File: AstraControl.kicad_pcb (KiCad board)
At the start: 4 copper layers, 110 x 96 mm, 149 parts, among them CN1 4P JST VH, CN10 JST_ZH_6PIN_1A_250V, CN2 4P JST VH, CN3 4P JST VH, CN4 4P JST ZH, CN5 4P JST ZH, CN6 4P JST ZH, CN7 JST_VH_8PIN_10A_250V, CN8 4P JST ZH, CN9 4P JST ZH, SW1 TS_Basic_Small, SW2 TS_Basic_Small, U1 ESP32-S3-WROOM-1U-N8, U2 NCP361SNT1G, U3 ST1S12GR, U4 USBLC6, U5 SN65HVD1782DR, U6 TXB0104PWR

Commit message: commit before updating to LiveAstra lib
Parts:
- removed H1, H2, H3, H4: MountingHole_Pad, MountingHole:MountingHole_5.3mm_M5_DIN965_Pad
- removed TP16, TP17: TestPoint_Thimble, TestPoint:TestPoint_Loop_D3.50mm_Drill0.9mm_Beaded
- added G1: ~, EASYEDA2KICAD:AstraControl_Ground_Band, F.Cu at (158.0, 108.0)
- added R9: 10k, Resistor_SMD:R_0402_1005Metric, F.Cu at (170.5, 143.0)
- moved R34 143.0 mm to (109.0, 80.0), turned to 180 degrees
- moved C23 137.9 mm to (109.0, 82.0), turned to 180 degrees
- moved R36 132.4 mm to (107.5, 138.0)
- moved R33 127.5 mm to (162.5, 142.5), turned to 90 degrees
- moved C25 127.5 mm to (107.5, 141.0)
- moved TP64 125.3 mm to (149.5, 142.5)
- moved C22 124.3 mm to (167.5, 143.5), turned to 90 degrees
- moved R32 123.6 mm to (165.5, 143.5), turned to 90 degrees
- moved TP18 118.7 mm to (116.5, 76.0)
- moved TP55 114.0 mm to (191.0, 78.5)
- moved TP59 110.2 mm to (178.0, 81.0)
- moved TP60 109.6 mm to (148.0, 135.0)
- moved TP56 107.7 mm to (183.0, 81.5)
- moved TP57 107.3 mm to (188.5, 82.0)
- moved TP1 106.9 mm to (130.0, 112.0)
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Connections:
- net Net-(CN9-Pad4) renamed /Block Diagram/Button, Status LED, UART and I2S/STATUS_LED_CONN
- net Net-(U1-IO3) renamed /Block Diagram/MCU/IO_3_IC
- CN9 pad 2: /Block Diagram/Button, Status LED, UART and I2S/GPIO_12_BUTTON -> Net-(CN9-Pad2)
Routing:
- net CHASSIS: track 0.00 -> 6.80 mm
- net GND: track 0.00 -> 0.58 mm
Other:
- outline, holes or cut-outs redrawn

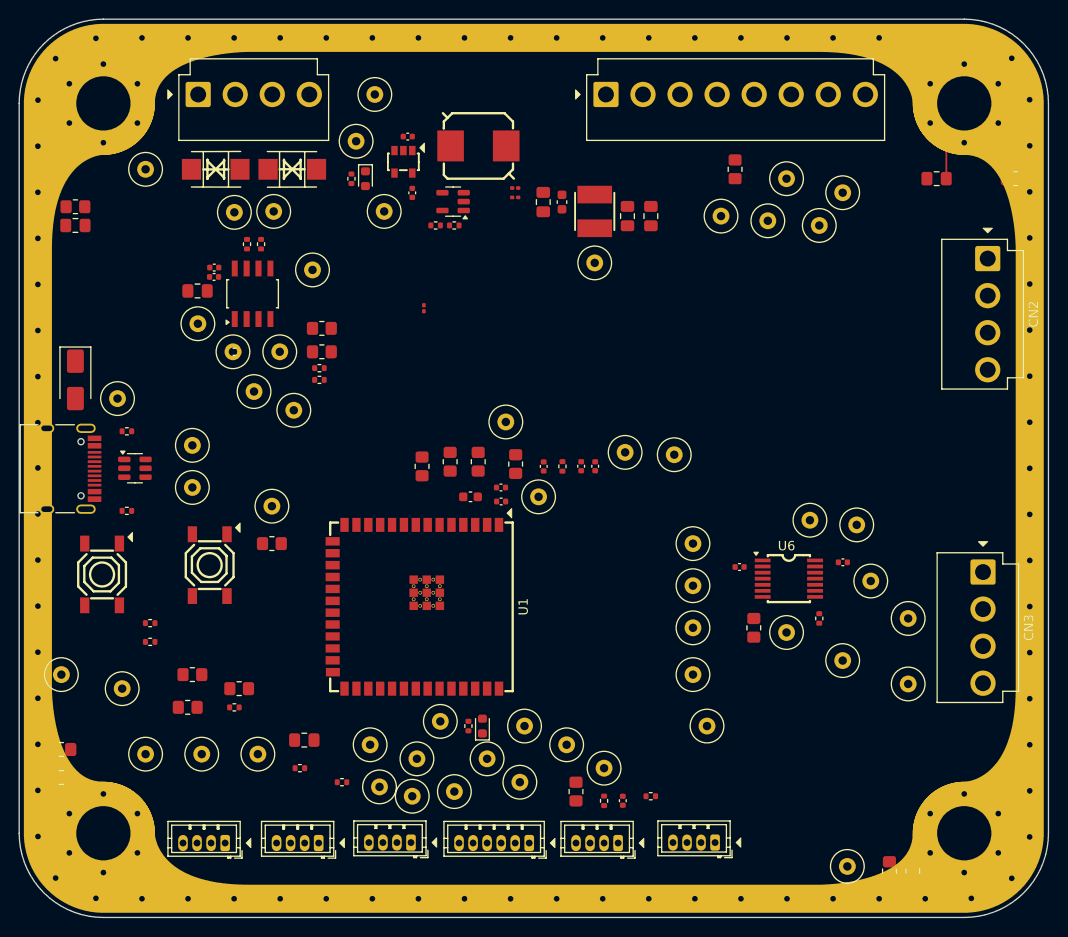
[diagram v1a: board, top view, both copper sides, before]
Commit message: Updated library name, updated and verified all footprints
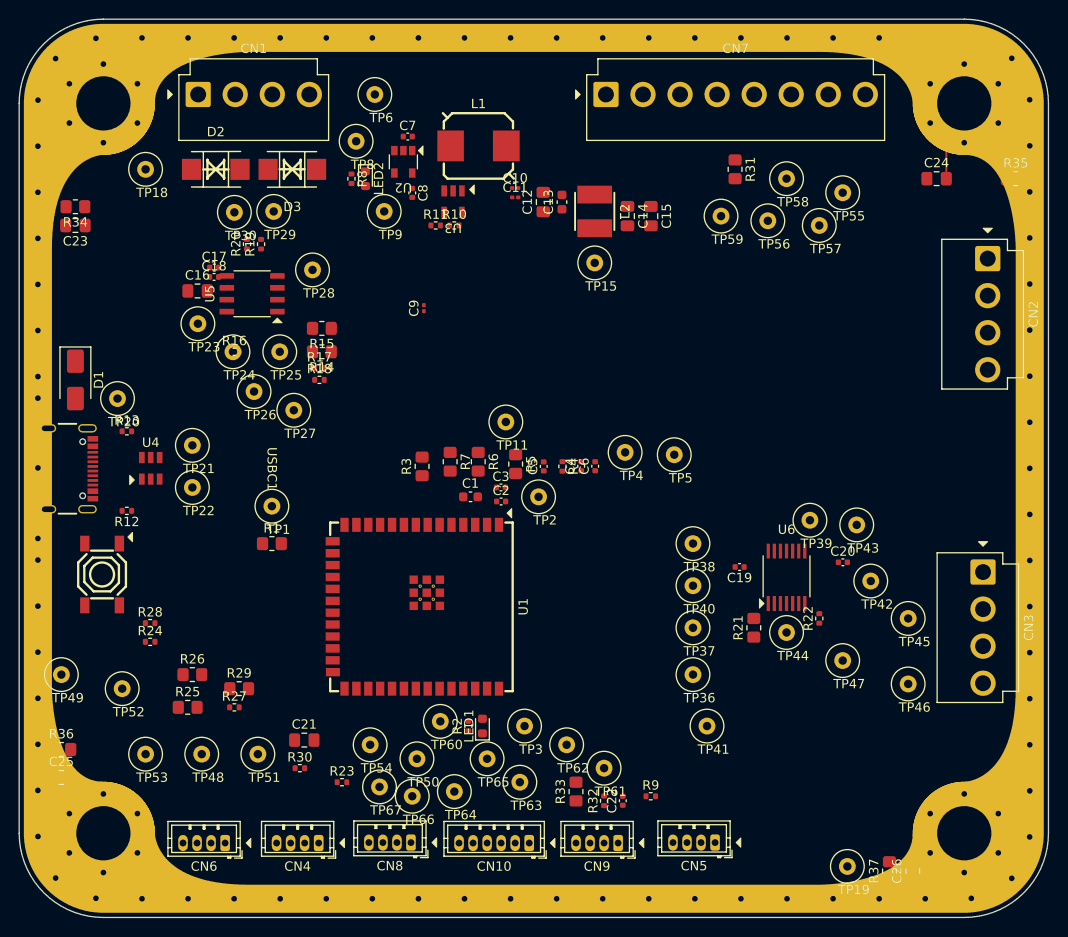
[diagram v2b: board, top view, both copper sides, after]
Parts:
- removed SW2: TS_Basic_Small, EASYEDA2KICAD:SW-SMD_4P-L5.1-W5.1-P3.70-LS6.5-TL-2
- CN1, CN2, CN3: footprint EASYEDA2KICAD:JST_VH_B4P-VH-B_1x04_P3.96mm_Vertical -> LiveAstra:JST_VH_B4P-VH-B_1x04_P3.96mm_Vertical
- D2, D3: footprint EASYEDA2KICAD:SMB_L4.6-W3.6-LS5.3-BI -> LiveAstra:SMB_L4.6-W3.6-LS5.3-BI
- G1: footprint EASYEDA2KICAD:AstraControl_Ground_Band -> LiveAstra:AstraControl_Ground_Band
- L1: value 4u7 -> 4u7H; footprint EASYEDA2KICAD:IND-SMD_L7.5-W7.0_SPM7054VT-330M-D -> LiveAstra:IND-SMD_L7.5-W7.0_SPM7054VT-330M-D
- L2: value 22u -> 22uH; footprint EASYEDA2KICAD:IND-SMD_L4.0-W4.0_SLW4010S -> LiveAstra:IND-SMD_L4.0-W4.0_SLW4010S
- LED1: value 19-213/Y2C-CQ2R2L/3T(CY) -> LED_Yellow_25mA_0603
- SW1: footprint EASYEDA2KICAD:SW-SMD_4P-L5.1-W5.1-P3.70-LS6.5-TL-2 -> LiveAstra:SW-SMD_4P-L5.1-W5.1-P3.70-LS6.5-TL-2
- U1: footprint EASYEDA2KICAD:WIRELM-SMD_ESP32-S3-WROOM-1U -> LiveAstra:WIRELM-SMD_ESP32-S3-WROOM-1U
- U2: footprint EASYEDA2KICAD:TSOP-5_L3.0-W1.5-P0.95-BL -> LiveAstra:5V_PROTECTION_NCP361SNT1G_TSOP-5
- U3: footprint Package_TO_SOT_SMD:TSOT-23-5 -> LiveAstra:STEP_DOWN_ST1S12GR_TSOT-23-5
- U4: footprint Package_TO_SOT_SMD:SOT-23-6 -> LiveAstra:USBLC6-4SC6_PROTECTION
- U5: footprint EASYEDA2KICAD:SOIC-8-R-PDSO-G8 -> LiveAstra:RS_485_SN65HVD1782DR
- U6: footprint EASYEDA2KICAD:TSSOP-14_L5.0-W4.4-P0.65-LS6.4-BL -> LiveAstra:LOGIC_SHIFTER_TXB0104PWR_TSOP_14
- USBC1: footprint Connector_USB:USB_C_Receptacle_HRO_TYPE-C-31-M-12 -> LiveAstra:USB_C_Korean_Hroparts_Elec_TYPE-C-31-M-12
- moved USBC1 3.00 mm to (104.0, 108.0)
- moved U4 1.69 mm to (117.0, 108.0)
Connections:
- SW1 pad 1: /Block Diagram/MCU Enable and Boot/BOOT_SW -> GND
- SW1 pad 4: GND -> /Block Diagram/MCU Enable and Boot/BOOT_SW

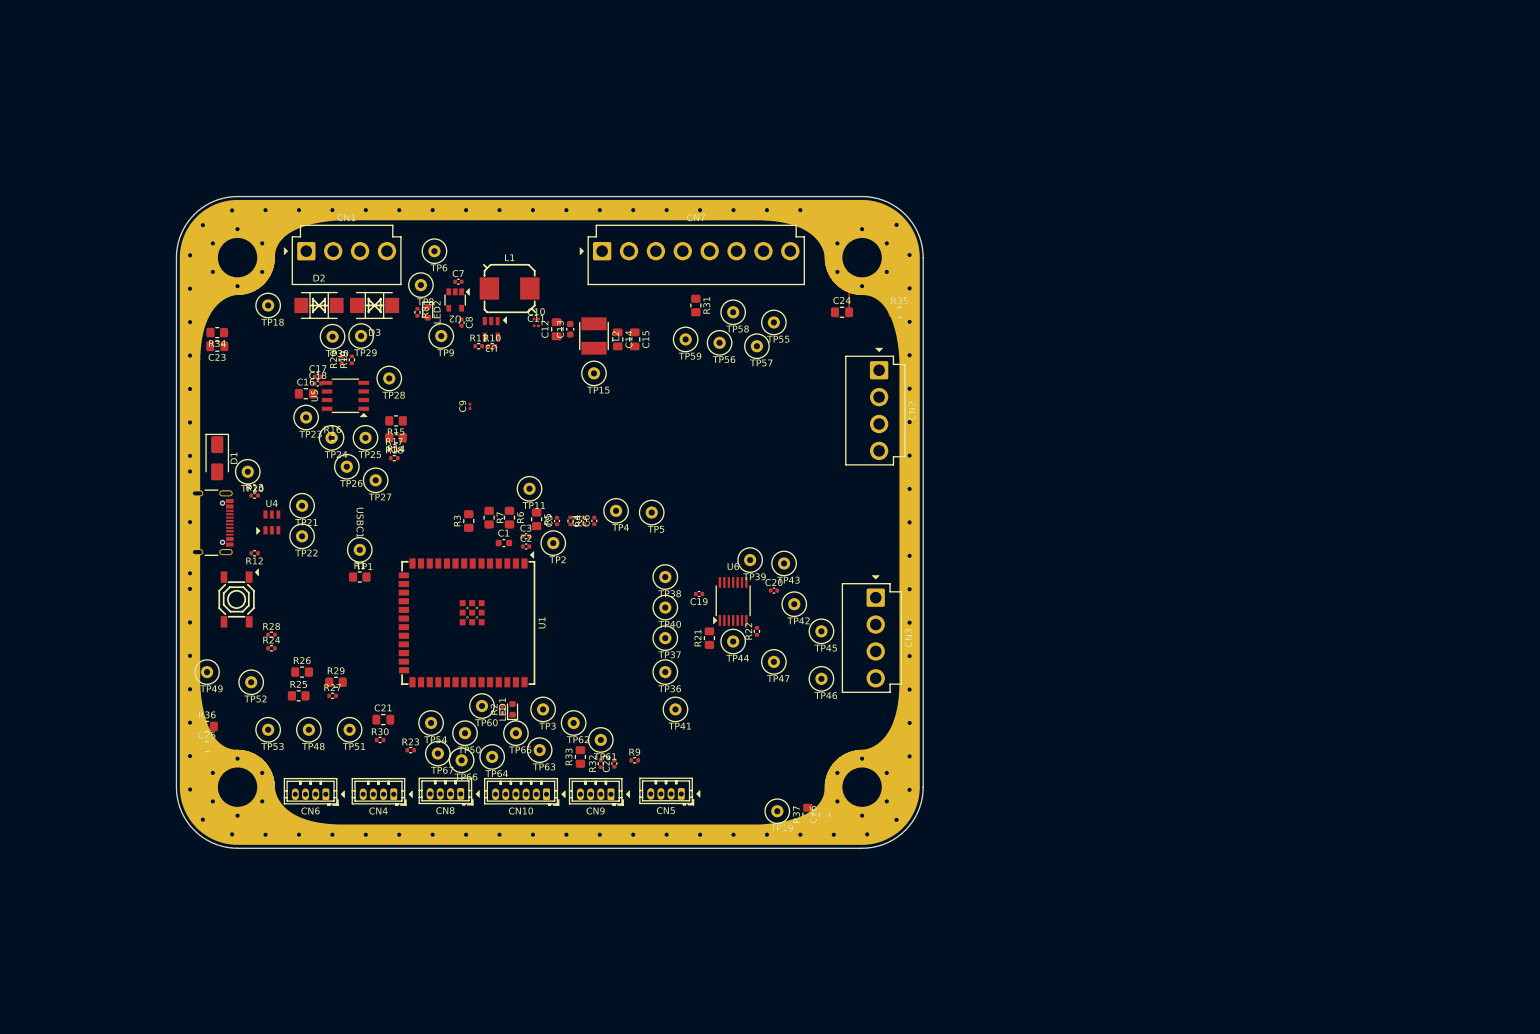
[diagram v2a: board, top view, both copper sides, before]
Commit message: Finished layout no drc or erc errors
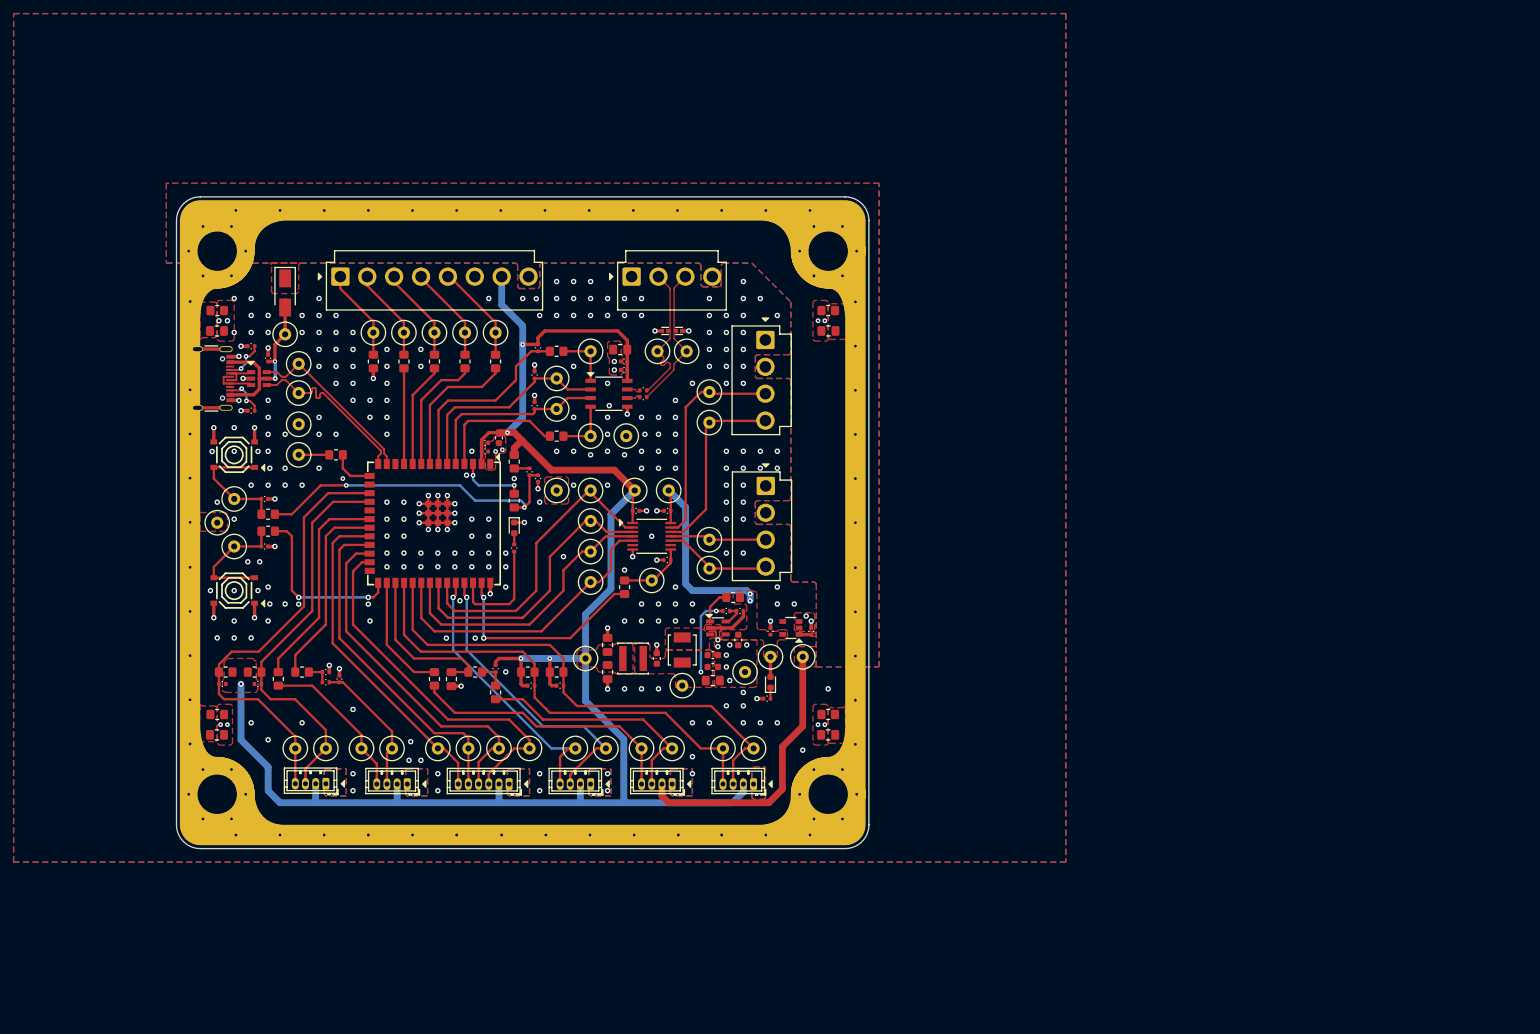
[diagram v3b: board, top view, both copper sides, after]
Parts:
- removed TP23, TP27, TP42, TP57, TP58, TP59, TP60, TP61, TP62, TP63, TP64, TP65, TP66, TP67: TestPoint_Thimble, TestPoint:TestPoint_Loop_D3.50mm_Drill0.9mm_Beaded
- removed U5: SN65HVD1782DR, LiveAstra:RS_485_SN65HVD1782DR
- added C27: 100n, LiveAstra:C_0402_1005Metric, F.Cu at (116.5, 83.8)
- added R38: 1M, LiveAstra:R_0805_2012Metric_Pad1.20x1.40mm_HandSolder, F.Cu at (109.0, 76.8)
- added R39: 0, LiveAstra:R_0805_2012Metric_Pad1.20x1.40mm_HandSolder, F.Cu at (145.5, 84.2)
- added R40: 0, LiveAstra:R_0805_2012Metric_Pad1.20x1.40mm_HandSolder, F.Cu at (141.0, 84.2)
- added R41: 0, LiveAstra:R_0805_2012Metric_Pad1.20x1.40mm_HandSolder, F.Cu at (136.5, 84.2)
- added R42: 0, LiveAstra:R_0805_2012Metric_Pad1.20x1.40mm_HandSolder, F.Cu at (150.0, 84.2)
- added R43: 0, LiveAstra:R_0805_2012Metric_Pad1.20x1.40mm_HandSolder, F.Cu at (154.8, 130.0)
- added R44: 0, LiveAstra:R_0805_2012Metric_Pad1.20x1.40mm_HandSolder, F.Cu at (159.0, 130.0)
- added R45: 0, LiveAstra:R_0805_2012Metric_Pad1.20x1.40mm_HandSolder, F.Cu at (114.5, 130.0)
- added R46: 0, LiveAstra:R_0805_2012Metric_Pad1.20x1.40mm_HandSolder, F.Cu at (110.2, 130.0)
- added R47: 0, LiveAstra:R_0805_2012Metric_Pad1.20x1.40mm_HandSolder, F.Cu at (121.5, 130.0)
- added SW2: TS_Basic_Small, LiveAstra:TACTILE_SWITCH-SMD_4P-L5.1-W5.1-P3.70-LS6.5-TL-2, F.Cu at (111.5, 98.0)
- added TP10: TestPoint_Thimble, LiveAstra:TestPoint_Loop_D3.50mm_Drill0.9mm_Beaded, F.Cu at (163.2, 128.0)
- added TP12: TestPoint_Thimble, LiveAstra:TestPoint_Loop_D3.50mm_Drill0.9mm_Beaded, F.Cu at (109.0, 108.0)
- added TP13: TestPoint_Thimble, LiveAstra:TestPoint_Loop_D3.50mm_Drill0.9mm_Beaded, F.Cu at (119.0, 80.2)
- added TP14: TestPoint_Thimble, LiveAstra:TestPoint_Loop_D3.50mm_Drill0.9mm_Beaded, F.Cu at (121.0, 84.6)
- added TP16: TestPoint_Thimble, LiveAstra:TestPoint_Loop_D3.50mm_Drill0.9mm_Beaded, F.Cu at (173.8, 82.8)
- added TP31: TestPoint_Thimble, LiveAstra:TestPoint_Loop_D3.50mm_Drill0.9mm_Beaded, F.Cu at (175.5, 103.2)
- added TP33: TestPoint_Thimble, LiveAstra:TestPoint_Loop_D3.50mm_Drill0.9mm_Beaded, F.Cu at (181.5, 93.2)
- added TP34: TestPoint_Thimble, LiveAstra:TestPoint_Loop_D3.50mm_Drill0.9mm_Beaded, F.Cu at (181.5, 110.5)
- added TP35: TestPoint_Thimble, LiveAstra:TestPoint_Loop_D3.50mm_Drill0.9mm_Beaded, F.Cu at (181.5, 114.8)
- added TP7: TestPoint_Thimble, LiveAstra:TestPoint_Loop_D3.50mm_Drill0.9mm_Beaded, F.Cu at (186.8, 130.0)
- added U7: USBLC6-2SC6, LiveAstra:USBLC6-2SC6_PROTECTION_SOT-23-6, F.Cu at (115.2, 86.8)
- C1, C13: footprint Capacitor_SMD:C_0603_1608Metric -> LiveAstra:C_0603_1608Metric
- C10, C11, C9: footprint Capacitor_SMD:C_0201_0603Metric -> LiveAstra:C_0603_1608Metric
- C12, C14, C15, C16, C21, C23, C24, C25, C26: footprint Capacitor_SMD:C_0805_2012Metric_Pad1.18x1.45mm_HandSolder -> LiveAstra:C_0805_2012Metric_Pad1.18x1.45mm_HandSolder
- C17, C18, C19, C2, C20, C22, C3, C4, C5, C6, C7, C8: footprint Capacitor_SMD:C_0402_1005Metric -> LiveAstra:C_0402_1005Metric
- CN10: footprint Connector_JST:JST_ZH_B6B-ZR_1x06_P1.50mm_Vertical -> LiveAstra:JST_ZH_B6B-ZR_1x06_P1.50mm_Vertical
- CN4, CN5, CN6, CN8, CN9: footprint Connector_JST:JST_ZH_B4B-ZR_1x04_P1.50mm_Vertical -> LiveAstra:JST_ZH_B4B-ZR_1x04_P1.50mm_Vertical
- CN7: footprint Connector_JST:JST_VH_B8P-VH-B_1x08_P3.96mm_Vertical -> LiveAstra:JST_VH_B8P-VH-B_1x08_P3.96mm_Vertical
- D1: footprint Diode_SMD:D_SMA -> LiveAstra:D_SMA_SS14_C2480
- D2, D3: value SMBJ43CA -> H5VL10B; footprint LiveAstra:SMB_L4.6-W3.6-LS5.3-BI -> LiveAstra:D_DFN0603_H5VL10B_Bidirectional_TVS
- L1: value 4u7H -> 2u2H; footprint LiveAstra:IND-SMD_L7.5-W7.0_SPM7054VT-330M-D -> LiveAstra:L_MDA4020_4.1x4.5mm
- L2: footprint LiveAstra:IND-SMD_L4.0-W4.0_SLW4010S -> LiveAstra:L_Sunlord_SWPA4030S
- LED1, LED2: footprint LED_SMD:LED_0603_1608Metric -> LiveAstra:LED_0603_1608Metric
- R1, R21, R25, R26, R29, R3, R31, R33, R35, R36, R37, R5, R6, R7: footprint Resistor_SMD:R_0805_2012Metric_Pad1.20x1.40mm_HandSolder -> LiveAstra:R_0805_2012Metric_Pad1.20x1.40mm_HandSolder
- R10, R11, R12, R13, R18, R2, R22, R23, R24, R27, R28, R30, R32, R4, R8: footprint Resistor_SMD:R_0402_1005Metric -> LiveAstra:R_0402_1005Metric
- R14, R15: value 0 -> 10; footprint Resistor_SMD:R_0805_2012Metric_Pad1.20x1.40mm_HandSolder -> LiveAstra:R_0402_1005Metric
- R16, R17: value 10k -> 0; footprint Resistor_SMD:R_0402_1005Metric -> LiveAstra:R_0805_2012Metric_Pad1.20x1.40mm_HandSolder
- R19, R20: value 10 -> 10k; footprint Resistor_SMD:R_0402_1005Metric -> LiveAstra:R_0402_1005Metric
- R34: value 1M -> 10k; footprint Resistor_SMD:R_0805_2012Metric_Pad1.20x1.40mm_HandSolder -> LiveAstra:R_0402_1005Metric
- R9: value 10k -> 1M; footprint Resistor_SMD:R_0402_1005Metric -> LiveAstra:R_0805_2012Metric_Pad1.20x1.40mm_HandSolder
- SW1: footprint LiveAstra:SW-SMD_4P-L5.1-W5.1-P3.70-LS6.5-TL-2 -> LiveAstra:TACTILE_SWITCH-SMD_4P-L5.1-W5.1-P3.70-LS6.5-TL-2
- TP1, TP11, TP15, TP18, TP19, TP2, TP20, TP21, TP22, TP24, TP25, TP26, TP28, TP29, TP3, TP30, TP36, TP37, TP38, TP39, TP4, TP40, TP41, TP43, TP44, TP45, TP46, TP47, TP48, TP49, TP5, TP50, TP51, TP52, TP53, TP54, TP55, TP56, TP6, TP8, TP9: footprint TestPoint:TestPoint_Loop_D3.50mm_Drill0.9mm_Beaded -> LiveAstra:TestPoint_Loop_D3.50mm_Drill0.9mm_Beaded
- U4: value USBLC6 -> SN65HVD1782DR; footprint LiveAstra:USBLC6-4SC6_PROTECTION -> LiveAstra:RS_485_SN65HVD1782DR
- moved R35 116.7 mm to (109.0, 136.2), turned to 180 degrees
- moved C26 114.4 mm to (109.0, 79.8), turned to 180 degrees
- moved C25 110.1 mm to (199.0, 79.8)
- moved R36 91.5 mm to (199.0, 136.2)
- moved TP46 83.4 mm to (132.0, 80.0)
- moved TP6 80.7 mm to (195.2, 127.8)
- moved R8 76.7 mm to (190.0, 133.9), turned to 0 degrees
- moved TP45 75.6 mm to (136.5, 80.0)
- moved R37 74.3 mm to (199.0, 76.8), turned to 0 degrees
- moved LED2 74.3 mm to (190.5, 131.5), turned to 90 degrees
- moved C7 73.2 mm to (196.5, 124.0), turned to -90 degrees
- moved TP19 73.1 mm to (164.0, 82.8)
- moved U2 69.1 mm to (193.5, 123.5), turned to -90 degrees
- moved TP9 67.7 mm to (190.5, 127.8)
- moved TP55 67.5 mm to (166.2, 141.2)
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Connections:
- net /Block Diagram/MCU Enable and Boot/EN_DELAY_R renamed /Block Diagram/MCU Enable and Boot/EN_DELAY_0
- net Net-(R1-Pad1) renamed /Block Diagram/MCU/IO_3_TEST
- net Net-(R26-Pad2) renamed /Block Diagram/Fan, Temperature and Screen/FAN_TACHO_0
- C10 pad 2: /Block Diagram/5V to 3.3V/SW_OUT_PRE_FILTER -> /Block Diagram/5V to 3.3V/SW_OUT_UNFILTERED
- C11 pad 2: /Block Diagram/5V to 3.3V/SW_OUT_PRE_FILTER -> /Block Diagram/5V to 3.3V/SW_OUT_UNFILTERED
- C12 pad 2: /Block Diagram/5V to 3.3V/SW_OUT_PRE_FILTER -> /Block Diagram/5V to 3.3V/SW_OUT_UNFILTERED
- C13 pad 2: /Block Diagram/5V to 3.3V/SW_OUT_PRE_FILTER -> /Block Diagram/5V to 3.3V/SW_OUT_UNFILTERED
- C22 pad 2: /Block Diagram/Button, Status LED, UART and I2S/GPIO_12_BUTTON -> /Block Diagram/Button, Status LED, UART and I2S/GPIO_12_BUTTON_CONN
- C4 pad 1: GND -> /Block Diagram/MCU Enable and Boot/EN_DELAY
- C4 pad 2: /Block Diagram/MCU Enable and Boot/EN_DELAY_C -> GND
- CN7 pad 1: +5V_IN -> /Block Diagram/LED PWM Connector/LED_GPIO_OR_GND_CONN
- CN7 pad 2: /Block Diagram/LED PWM Connector/GPIO_39_PWM_CH1 -> /Block Diagram/LED PWM Connector/LED_GPIO_40_CONN
- CN7 pad 3: /Block Diagram/LED PWM Connector/GPIO_40_PWM_CH2 -> /Block Diagram/LED PWM Connector/LED_GPIO_43_CONN
- CN7 pad 4: /Block Diagram/LED PWM Connector/GPIO_41_PWM_CH3 -> /Block Diagram/LED PWM Connector/LED_GPIO_42_CONN
- CN7 pad 5: /Block Diagram/LED PWM Connector/GPIO_42_PWM_CH4 -> /Block Diagram/LED PWM Connector/LED_GPIO_39_CONN
- CN7 pad 6: /Block Diagram/LED PWM Connector/LED_PWM_CONN_GND -> GND
- CN7 pad 8: GND -> +5V_IN
- CN9 pad 2: Net-(CN9-Pad2) -> +3V3
- CN9 pad 3: +3V3 -> /Block Diagram/Button, Status LED, UART and I2S/GPIO_12_BUTTON_CONN
- CN9 pad 4: /Block Diagram/Button, Status LED, UART and I2S/STATUS_LED_CONN -> /Block Diagram/Button, Status LED, UART and I2S/GPIO_13_STATUS_LED_CONN
- D2 pad 1: CHASSIS -> GND
- D3 pad 1: CHASSIS -> GND
- L1 pad 2: /Block Diagram/5V to 3.3V/SW_OUT_PRE_FILTER -> /Block Diagram/5V to 3.3V/SW_OUT_UNFILTERED
- L2 pad 1: /Block Diagram/5V to 3.3V/SW_OUT_PRE_FILTER -> /Block Diagram/5V to 3.3V/SW_OUT_UNFILTERED
- R10 pad 2: /Block Diagram/5V to 3.3V/SW_OUT_PRE_FILTER -> /Block Diagram/5V to 3.3V/SW_OUT_UNFILTERED
- R14 pad 1: /Block Diagram/UART to RS-485/TX -> /Block Diagram/Power Connectors/RS485_D-
- R14 pad 2: /Block Diagram/UART to RS-485/D_IC -> /Block Diagram/UART to RS-485/RS485_IC_D-
- R15 pad 1: /Block Diagram/UART to RS-485/RX -> /Block Diagram/Power Connectors/RS485_D+
- R15 pad 2: /Block Diagram/UART to RS-485/R_IC -> /Block Diagram/UART to RS-485/RS485_IC_D+
- R16 pad 1: /Block Diagram/UART to RS-485/R_IC -> /Block Diagram/UART to RS-485/RS485_RX_IC
- R16 pad 2: +3V3 -> /Block Diagram/MCU/GPIO_18_RS485_RX
- R17 pad 1: GND -> /Block Diagram/UART to RS-485/RS485_TX_IC
- R17 pad 2: /Block Diagram/MCU/GPIO_15_RS485_RE -> /Block Diagram/MCU/GPIO_17_RS485_TX
- R19 pad 1: /Block Diagram/UART to RS-485/IC_D- -> GND
- R19 pad 2: /Block Diagram/Power Connectors/RS485_D- -> /Block Diagram/MCU/GPIO_15_RS485_RE
- R20 pad 1: /Block Diagram/UART to RS-485/IC_D+ -> /Block Diagram/MCU/GPIO_18_RS485_RX
- R20 pad 2: /Block Diagram/Power Connectors/RS485_D+ -> +3V3
- R21 pad 1: /Block Diagram/3V3 to 5V Logic Shifter/OE -> /Block Diagram/3V3 to 5V Logic Shifter/LEVEL_SHIFTER_IO_OE
- R31 pad 2: /Block Diagram/LED PWM Connector/LED_PWM_CONN_GND -> /Block Diagram/LED PWM Connector/LED_GPIO_OR_GND_CONN
- R32 pad 2: /Block Diagram/Button, Status LED, UART and I2S/GPIO_12_BUTTON -> /Block Diagram/Button, Status LED, UART and I2S/GPIO_12_BUTTON_0
- R33 pad 2: /Block Diagram/Button, Status LED, UART and I2S/STATUS_LED_CONN -> /Block Diagram/Button, Status LED, UART and I2S/GPIO_13_STATUS_LED_CONN
- R34 pad 1: GND -> /Block Diagram/Button, Status LED, UART and I2S/GPIO_12_BUTTON_CONN
- R34 pad 2: CHASSIS -> /Block Diagram/Button, Status LED, UART and I2S/GPIO_12_BUTTON_0
- R4 pad 1: /Block Diagram/MCU Enable and Boot/EN_DELAY_C -> /Block Diagram/MCU Enable and Boot/EN_DELAY
- R5 pad 2: +3V3 -> /Block Diagram/MCU Enable and Boot/EN_DELAY
- R6 pad 2: +3V3 -> /Block Diagram/MCU Enable and Boot/EN_DELAY
- R9 pad 1: Net-(CN9-Pad2) -> /Block Diagram/5V to 3.3V/EN
- R9 pad 2: /Block Diagram/Button, Status LED, UART and I2S/GPIO_12_BUTTON -> +5V
- SW1 pad 2: unconnected-(SW1-B-Pad2) -> /Block Diagram/MCU Enable and Boot/BOOT_SW
- TP11 pad 1: +5V -> GND
- TP15 pad 1: +3V3 -> /Block Diagram/MCU/USB_D+
- TP19 pad 1: CHASSIS -> /Block Diagram/UART to RS-485/RS485_RX_IC
- TP2 pad 1: +3V3 -> /Block Diagram/Power Connectors/RS485_D-
- TP20 pad 1: /Block Diagram/5V Protection/VBUS -> /Block Diagram/UART to RS-485/RS485_TX_IC
- TP21 pad 1: /Block Diagram/Power Connectors/USB/D- -> /Block Diagram/MCU/GPIO_15_RS485_RE
- TP22 pad 1: /Block Diagram/Power Connectors/USB/D+ -> /Block Diagram/MCU/GPIO_15_RS485_DE
- TP24 pad 1: /Block Diagram/UART to RS-485/R_IC -> /Block Diagram/3V3 to 5V Logic Shifter/3V3_IO_4
- TP25 pad 1: /Block Diagram/UART to RS-485/D_IC -> /Block Diagram/3V3 to 5V Logic Shifter/3V3_IO_3
- TP26 pad 1: /Block Diagram/MCU/GPIO_15_RS485_RE -> /Block Diagram/3V3 to 5V Logic Shifter/3V3_IO_2
- TP28 pad 1: GND -> /Block Diagram/3V3 to 5V Logic Shifter/OE_IC
- TP29 pad 1: /Block Diagram/Power Connectors/RS485_D- -> /Block Diagram/3V3 to 5V Logic Shifter/3V3_IO_1
- TP30 pad 1: /Block Diagram/Power Connectors/RS485_D+ -> /Block Diagram/3V3 to 5V Logic Shifter/5V_IO_1
- TP36 pad 1: /Block Diagram/3V3 to 5V Logic Shifter/3V3_IO_4 -> /Block Diagram/Fan, Temperature and Screen/FAN_PWM_CON
- TP37 pad 1: /Block Diagram/3V3 to 5V Logic Shifter/3V3_IO_3 -> /Block Diagram/Fan, Temperature and Screen/SCREEN_I2C_SCL
- TP38 pad 1: /Block Diagram/3V3 to 5V Logic Shifter/3V3_IO_2 -> /Block Diagram/Fan, Temperature and Screen/TEMP_I2C_SCL
- TP39 pad 1: +3V3 -> /Block Diagram/Fan, Temperature and Screen/FAN_TACHO_CON
- TP4 pad 1: +3V3 -> /Block Diagram/MCU Enable and Boot/EN_SW
- TP40 pad 1: /Block Diagram/3V3 to 5V Logic Shifter/OE_IC -> /Block Diagram/Fan, Temperature and Screen/SCREEN_I2C_SDA
- TP41 pad 1: /Block Diagram/3V3 to 5V Logic Shifter/3V3_IO_1 -> /Block Diagram/Fan, Temperature and Screen/TEMP_I2C_SDA
- TP43 pad 1: +5V -> /Block Diagram/LED PWM Connector/LED_GPIO_42_CONN
- TP44 pad 1: GND -> /Block Diagram/LED PWM Connector/LED_GPIO_43_CONN
- TP45 pad 1: /Block Diagram/3V3 to 5V Logic Shifter/5V_IO_2 -> /Block Diagram/LED PWM Connector/LED_GPIO_40_CONN
- TP46 pad 1: /Block Diagram/3V3 to 5V Logic Shifter/5V_IO_3 -> /Block Diagram/LED PWM Connector/LED_GPIO_OR_GND_CONN
- TP47 pad 1: /Block Diagram/3V3 to 5V Logic Shifter/5V_IO_4 -> /Block Diagram/LED PWM Connector/LED_GPIO_39_CONN
- TP48 pad 1: /Block Diagram/Fan, Temperature and Screen/FAN_PWM -> /Block Diagram/Button, Status LED, UART and I2S/UART_RX
- TP49 pad 1: /Block Diagram/Fan, Temperature and Screen/SCREEN_I2C_SCL -> /Block Diagram/Button, Status LED, UART and I2S/GPIO_12_BUTTON_CONN
- TP50 pad 1: /Block Diagram/Fan, Temperature and Screen/TEMP_I2C_SCL -> /Block Diagram/Button, Status LED, UART and I2S/GPIO_13_STATUS_LED_CONN
- TP51 pad 1: /Block Diagram/Fan, Temperature and Screen/FAN_TACHO_CON -> /Block Diagram/Button, Status LED, UART and I2S/GPIO_47_I2S_SD
- TP52 pad 1: /Block Diagram/Fan, Temperature and Screen/SCREEN_I2C_SDA -> /Block Diagram/Button, Status LED, UART and I2S/GPIO_21_I2S_SCK
- TP53 pad 1: /Block Diagram/Fan, Temperature and Screen/TEMP_I2C_SDA -> /Block Diagram/Button, Status LED, UART and I2S/GPIO_14_I2S_WS
- TP54 pad 1: /Block Diagram/Fan, Temperature and Screen/FAN_TACHO -> /Block Diagram/Button, Status LED, UART and I2S/GPIO_48_I2S_LR
- TP55 pad 1: /Block Diagram/LED PWM Connector/GPIO_42_PWM_CH4 -> /Block Diagram/Button, Status LED, UART and I2S/UART_TX
- TP56 pad 1: /Block Diagram/LED PWM Connector/GPIO_41_PWM_CH3 -> /Block Diagram/5V to 3.3V/SW_OUT_UNFILTERED
- TP8 pad 1: GND -> +3V3
- U1 pad 10: /Block Diagram/UART to RS-485/TX -> /Block Diagram/LED PWM Connector/GPIO_41_PWM_CH3
- U1 pad 11: /Block Diagram/UART to RS-485/RX -> /Block Diagram/LED PWM Connector/GPIO_40_PWM_CH2
- U1 pad 12: /Block Diagram/3V3 to 5V Logic Shifter/OE -> unconnected-(U1-IO8-Pad12)
- U1 pad 13: /Block Diagram/Power Connectors/USB/D- -> /Block Diagram/MCU/USB_D-
- U1 pad 14: /Block Diagram/Power Connectors/USB/D+ -> /Block Diagram/MCU/USB_D+
- U1 pad 20: /Block Diagram/Button, Status LED, UART and I2S/GPIO_12_BUTTON -> /Block Diagram/Button, Status LED, UART and I2S/GPIO_13_STATUS_LED
- U1 pad 21: /Block Diagram/Button, Status LED, UART and I2S/GPIO_13_STATUS_LED -> /Block Diagram/Button, Status LED, UART and I2S/GPIO_12_BUTTON
- U1 pad 22: /Block Diagram/Button, Status LED, UART and I2S/GPIO_14_I2S_WS -> /Block Diagram/Button, Status LED, UART and I2S/GPIO_48_I2S_LR
- U1 pad 23: /Block Diagram/Button, Status LED, UART and I2S/GPIO_21_I2S_SCK -> /Block Diagram/Button, Status LED, UART and I2S/GPIO_14_I2S_WS
- U1 pad 24: /Block Diagram/Button, Status LED, UART and I2S/GPIO_47_I2S_SD -> /Block Diagram/Button, Status LED, UART and I2S/GPIO_21_I2S_SCK
- U1 pad 25: /Block Diagram/Button, Status LED, UART and I2S/GPIO_48_I2S_LR -> /Block Diagram/Button, Status LED, UART and I2S/GPIO_47_I2S_SD
- U1 pad 28: /Block Diagram/3V3 to 5V Logic Shifter/3V3_IO_1 -> /Block Diagram/Fan, Temperature and Screen/FAN_PWM
- U1 pad 29: /Block Diagram/3V3 to 5V Logic Shifter/3V3_IO_2 -> /Block Diagram/Fan, Temperature and Screen/FAN_TACHO
- U1 pad 30: /Block Diagram/3V3 to 5V Logic Shifter/3V3_IO_3 -> /Block Diagram/Fan, Temperature and Screen/TEMP_I2C_SCL
- U1 pad 31: /Block Diagram/3V3 to 5V Logic Shifter/3V3_IO_4 -> /Block Diagram/Fan, Temperature and Screen/TEMP_I2C_SDA
- U1 pad 32: /Block Diagram/LED PWM Connector/GPIO_39_PWM_CH1 -> /Block Diagram/3V3 to 5V Logic Shifter/3V3_IO_4
- U1 pad 33: /Block Diagram/LED PWM Connector/GPIO_40_PWM_CH2 -> /Block Diagram/3V3 to 5V Logic Shifter/3V3_IO_3
- U1 pad 34: /Block Diagram/LED PWM Connector/GPIO_41_PWM_CH3 -> /Block Diagram/3V3 to 5V Logic Shifter/3V3_IO_2
- U1 pad 35: /Block Diagram/LED PWM Connector/GPIO_42_PWM_CH4 -> /Block Diagram/3V3 to 5V Logic Shifter/3V3_IO_1
- U1 pad 39: unconnected-(U1-IO1-Pad39) -> /Block Diagram/3V3 to 5V Logic Shifter/LEVEL_SHIFTER_IO_OE
- U1 pad 4: /Block Diagram/Fan, Temperature and Screen/FAN_TACHO -> /Block Diagram/MCU/GPIO_17_RS485_TX
- U1 pad 5: /Block Diagram/Fan, Temperature and Screen/FAN_PWM -> /Block Diagram/MCU/GPIO_15_RS485_DE
- U1 pad 6: /Block Diagram/Fan, Temperature and Screen/TEMP_I2C_SCL -> /Block Diagram/MCU/GPIO_15_RS485_RE
- U1 pad 7: /Block Diagram/Fan, Temperature and Screen/TEMP_I2C_SDA -> /Block Diagram/MCU/GPIO_18_RS485_RX
- U1 pad 8: /Block Diagram/MCU/GPIO_15_RS485_DE -> /Block Diagram/LED PWM Connector/GPIO_39_PWM_CH1
- U1 pad 9: /Block Diagram/MCU/GPIO_15_RS485_RE -> /Block Diagram/LED PWM Connector/GPIO_42_PWM_CH4
- U3 pad 1: +5V -> /Block Diagram/5V to 3.3V/EN
- U4 pad 1: /Block Diagram/Power Connectors/USB/D- -> /Block Diagram/UART to RS-485/RS485_RX_IC
- U4 pad 2: GND -> /Block Diagram/MCU/GPIO_15_RS485_RE
- U4 pad 3: /Block Diagram/Power Connectors/USB/D+ -> /Block Diagram/MCU/GPIO_15_RS485_DE
- U4 pad 4: /Block Diagram/Power Connectors/USB/D+ -> /Block Diagram/UART to RS-485/RS485_TX_IC
- U4 pad 5: /Block Diagram/5V Protection/VBUS -> GND
- U4 pad 6: /Block Diagram/Power Connectors/USB/D- -> /Block Diagram/UART to RS-485/RS485_IC_D-
- USBC1 pad A6: /Block Diagram/Power Connectors/USB/D+ -> /Block Diagram/Power Connectors/USB/USB_CONN_D+
- USBC1 pad A7: /Block Diagram/Power Connectors/USB/D- -> /Block Diagram/Power Connectors/USB/USB_CONN_D-
- USBC1 pad B6: /Block Diagram/Power Connectors/USB/D+ -> /Block Diagram/Power Connectors/USB/USB_CONN_D+
- USBC1 pad B7: /Block Diagram/Power Connectors/USB/D- -> /Block Diagram/Power Connectors/USB/USB_CONN_D-
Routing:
- net +3V3: track 0.00 -> 262.1 mm, vias 0 -> 5
- net GND: track 0.58 -> 80.3 mm, vias 0 -> 301
- net /Block Diagram/Fan, Temperature and Screen/TEMP_I2C_SDA: track 0.00 -> 74.5 mm
- net /Block Diagram/Fan, Temperature and Screen/TEMP_I2C_SCL: track 0.00 -> 69.8 mm
- net /Block Diagram/Fan, Temperature and Screen/SCREEN_I2C_SCL: track 0.00 -> 65.5 mm
- net /Block Diagram/Fan, Temperature and Screen/SCREEN_I2C_SDA: track 0.00 -> 58.5 mm
- net /Block Diagram/Button, Status LED, UART and I2S/GPIO_47_I2S_SD: track 0.00 -> 54.2 mm
- net /Block Diagram/Button, Status LED, UART and I2S/GPIO_21_I2S_SCK: track 0.00 -> 51.7 mm
- net /Block Diagram/Button, Status LED, UART and I2S/GPIO_14_I2S_WS: track 0.00 -> 49.7 mm
- net /Block Diagram/Button, Status LED, UART and I2S/GPIO_48_I2S_LR: track 0.00 -> 49.5 mm
- net /Block Diagram/MCU Enable and Boot/EN_DELAY: track 0.00 -> 47.9 mm, vias 0 -> 2
- net /Block Diagram/Button, Status LED, UART and I2S/UART_TX: track 0.00 -> 45.3 mm, vias 0 -> 1
- net /Block Diagram/3V3 to 5V Logic Shifter/3V3_IO_1: track 0.00 -> 44.7 mm
- net /Block Diagram/3V3 to 5V Logic Shifter/3V3_IO_4: track 0.00 -> 44.5 mm
- net +5V_IN: track 0.00 -> 43.3 mm
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- added copper zone on F.Cu, net +3V3
- added copper zone on F.Cu, net +5V
- added copper zone on B.Cu, net +5V_IN
- added copper zone on F.Cu, net +5V_IN
- added copper zone on F.Cu, net /Block Diagram/5V to 3.3V/SW_OUT
- added copper zone on F.Cu, net /Block Diagram/5V to 3.3V/SW_OUT_UNFILTERED
- added copper zone on F.Cu, net CHASSIS
- added copper zone on B.Cu, net GND
- added copper zone on F.Cu, net GND
- added copper zone on In1.Cu, net GND
- added copper zone on In2.Cu, net GND
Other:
- board size 110 x 96 mm -> 102 x 96 mm

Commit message: initial silkscreen work
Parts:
- moved TP11 33.4 mm to (131.5, 122.2)
- moved TP13 2.00 mm to (121.0, 80.2)
- moved D1 0.50 mm to (119.5, 74.2)
- moved TP9 0.25 mm to (190.5, 127.5)
- renumbered TP3 to TP11, TP11 to TP3
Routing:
- net /Block Diagram/MCU Enable and Boot/MCU_BOOT: track 25.7 -> 26.5 mm
- net GND: track 80.3 -> 80.9 mm
